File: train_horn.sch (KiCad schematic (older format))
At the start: 72 parts, among them J1 USB_OTG, J2 PROG, Q1 2N7002, SW1 PLAY, U1 MIC7221, U2 MCP73831, U3 TPS78233DDCR, U4 MSP430FR2000_TSSOP, U5 TPA6211A1

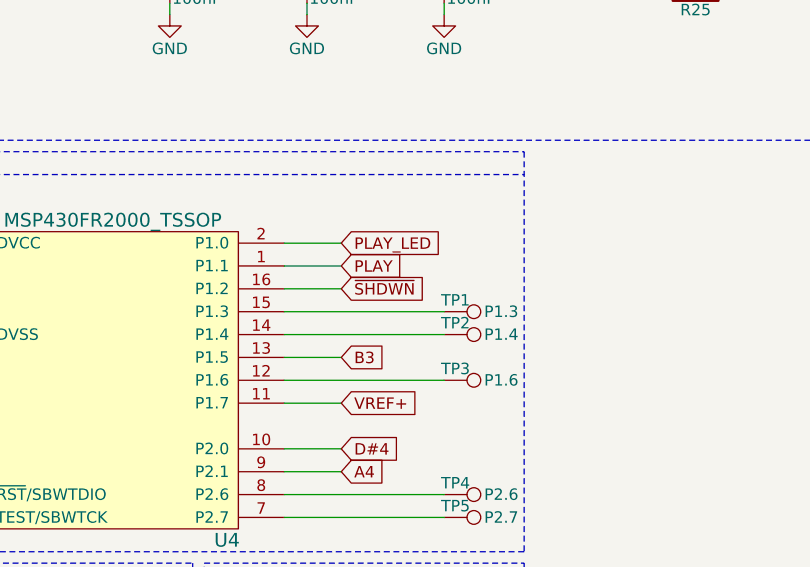
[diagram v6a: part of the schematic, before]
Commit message: move play button to P1.3 for PCB layout reasons
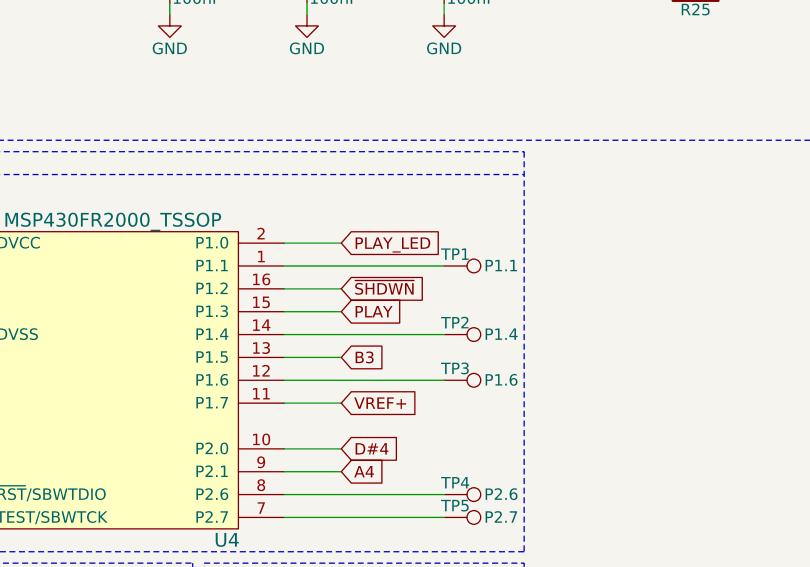
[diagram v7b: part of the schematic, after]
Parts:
- TP1: value P1.3 -> P1.1
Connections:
- net PLAY: now also U4.15 (P1.3); no longer U4.1 (P1.1)
- net at TP1.1: now also U4.1 (P1.1); no longer U4.15 (P1.3)
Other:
- moved on the sheet: TP1
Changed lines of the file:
@@
 Text GLabel 6600 3750 2    50   Input ~ 0
 PLAY_LED
-Text GLabel 6600 3850 2    50   Input ~ 0
+Text GLabel 6600 4050 2    50   Input ~ 0
 PLAY
 Text Notes 6000 5250 0    60   ~ 0
@@
 L Test_Point TP1
 U 1 1 5A824476
-P 7050 4050
-F 0 "TP1" V 7000 4100 50  0000 C CNN
-F 1 "P1.3" V 7050 4300 50  0000 C CNN
-F 2 "Connectors_TestPoints:Test_Point_Pad_d1.5mm" H 7250 4050 50  0001 C CNN
-F 3 "" H 7250 4050 50  0001 C CNN
-F 4 "NONE" H 7050 4050 60  0001 C CNN "Manufacture"
-F 5 "NONE" H 7050 4050 60  0001 C CNN "Mfg Part Number"
-F 6 "NONE" H 7050 4050 60  0001 C CNN "Package"
-F 7 "NONE" H 7050 4050 60  0001 C CNN "Description"
-	1    7050 4050
+P 7050 3850
+F 0 "TP1" V 7000 3900 50  0000 C CNN
+F 1 "P1.1" V 7050 4100 50  0000 C CNN
+F 2 "Connectors_TestPoints:Test_Point_Pad_d1.5mm" H 7250 3850 50  0001 C CNN
+F 3 "" H 7250 3850 50  0001 C CNN
+F 4 "NONE" H 7050 3850 60  0001 C CNN "Manufacture"
+F 5 "NONE" H 7050 3850 60  0001 C CNN "Mfg Part Number"
+F 6 "NONE" H 7050 3850 60  0001 C CNN "Package"
+F 7 "NONE" H 7050 3850 60  0001 C CNN "Description"
+	1    7050 3850
 	0    1    1    0
 $EndComp
@@
 	8750 1950 8800 1950
 Wire Wire Line
-	6350 3850 6600 3850
-Wire Wire Line
 	6450 5900 6800 5900
 Wire Wire Line
@@
 Wire Notes Line
 	6000 5150 7400 5150
-Wire Wire Line
-	6350 4050 7050 4050
 Wire Wire Line
 	7050 4150 6350 4150
@@
 Wire Wire Line
 	9800 1750 10100 1750
+Wire Wire Line
+	6350 4050 6600 4050
+Wire Wire Line
+	6350 3850 7050 3850
 $EndSCHEMATC

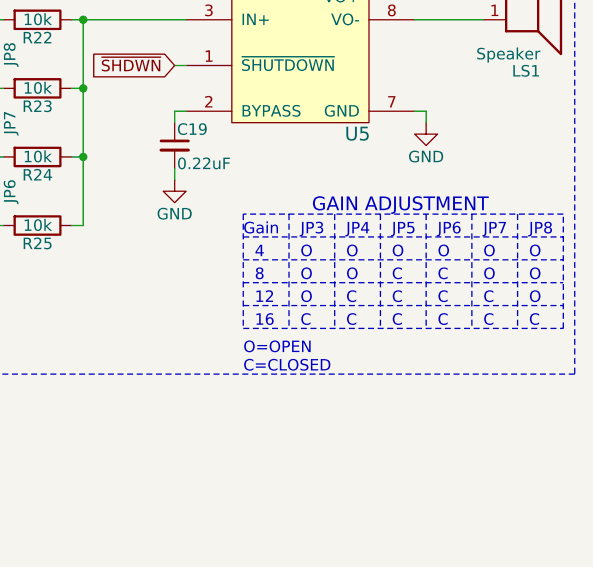
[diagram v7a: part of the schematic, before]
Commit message: finising touches on silkscreen
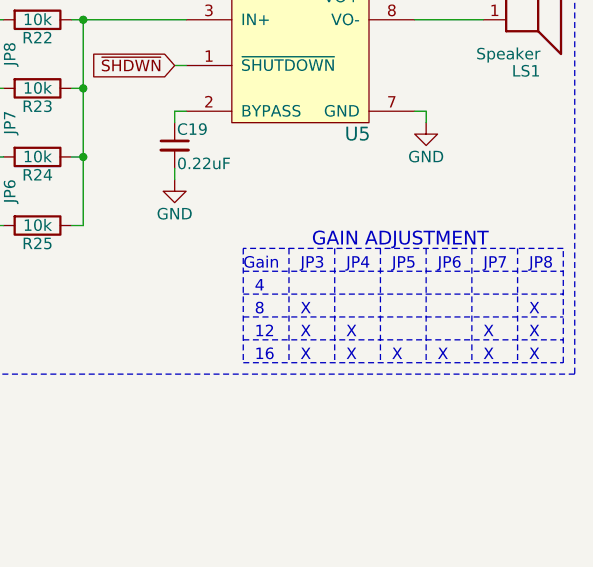
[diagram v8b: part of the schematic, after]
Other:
- note added: "X"
- note removed: "C"
- note removed: "O"
- note removed: "O=OPEN\nC=CLOSED"
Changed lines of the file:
@@
 	0    1    1    0
 $EndComp
-Text Notes 9050 2700 0    50   ~ 0
+Text Notes 9050 2850 0    50   ~ 0
 Gain
-Text Notes 9100 2800 0    50   ~ 0
+Text Notes 9100 2950 0    50   ~ 0
 4
-Text Notes 9100 2900 0    50   ~ 0
+Text Notes 9100 3050 0    50   ~ 0
 8
-Text Notes 9100 3000 0    50   ~ 0
+Text Notes 9100 3150 0    50   ~ 0
 12
-Text Notes 9100 3100 0    50   ~ 0
+Text Notes 9100 3250 0    50   ~ 0
 16
-Text Notes 9300 2700 0    50   ~ 0
+Text Notes 9300 2850 0    50   ~ 0
 JP3
-Text Notes 9700 2700 0    50   ~ 0
+Text Notes 9700 2850 0    50   ~ 0
 JP5
-Text Notes 9900 2700 0    50   ~ 0
+Text Notes 9900 2850 0    50   ~ 0
 JP6
-Text Notes 10100 2700 0    50   ~ 0
+Text Notes 10100 2850 0    50   ~ 0
 JP7
-Text Notes 10300 2700 0    50   ~ 0
+Text Notes 10300 2850 0    50   ~ 0
 JP8
-Text Notes 9300 2800 0    50   ~ 0
-O
-Text Notes 9500 2700 0    50   ~ 0
+Text Notes 9500 2850 0    50   ~ 0
 JP4
-Text Notes 9300 3100 0    50   ~ 0
-C
-Text Notes 9050 3300 0    50   ~ 0
-O=OPEN\nC=CLOSED
-Text Notes 9500 2800 0    50   ~ 0
-O
-Text Notes 9700 2800 0    50   ~ 0
-O
-Text Notes 9900 2800 0    50   ~ 0
-O
-Text Notes 10100 2800 0    50   ~ 0
-O
-Text Notes 10300 2800 0    50   ~ 0
-O
-Text Notes 9500 3100 0    50   ~ 0
-C
-Text Notes 9700 3100 0    50   ~ 0
-C
-Text Notes 9900 3100 0    50   ~ 0
-C
-Text Notes 10100 3100 0    50   ~ 0
-C
-Text Notes 10300 3100 0    50   ~ 0
-C
-Text Notes 9350 2600 0    60   ~ 0
+Text Notes 9300 3250 0    50   ~ 0
+X
+Text Notes 9500 3250 0    50   ~ 0
+X
+Text Notes 9700 3250 0    50   ~ 0
+X
+Text Notes 9900 3250 0    50   ~ 0
+X
+Text Notes 10100 3250 0    50   ~ 0
+X
+Text Notes 10300 3250 0    50   ~ 0
+X
+Text Notes 9350 2750 0    60   ~ 0
 GAIN ADJUSTMENT
-Text Notes 9700 2900 0    50   ~ 0
-C
-Text Notes 9900 2900 0    50   ~ 0
-C
-Text Notes 9700 3000 0    50   ~ 0
-C
-Text Notes 9900 3000 0    50   ~ 0
-C
-Text Notes 9500 3000 0    50   ~ 0
-C
-Text Notes 10100 3000 0    50   ~ 0
-C
-Text Notes 10100 2900 0    50   ~ 0
-O
-Text Notes 10300 2900 0    50   ~ 0
-O
-Text Notes 10300 3000 0    50   ~ 0
-O
-Text Notes 9500 2900 0    50   ~ 0
-O
-Text Notes 9300 2900 0    50   ~ 0
-O
-Text Notes 9300 3000 0    50   ~ 0
-O
+Text Notes 9500 3150 0    50   ~ 0
+X
+Text Notes 10100 3150 0    50   ~ 0
+X
+Text Notes 9300 3150 0    50   ~ 0
+X
 Wire Wire Line
 	4250 3750 4850 3750
@@
 Connection ~ 8350 1750
 Wire Notes Line
-	9050 2700 10450 2700
-Wire Notes Line
-	10250 2600 10250 3100
-Wire Notes Line
-	10050 2600 10050 3100
-Wire Notes Line
-	9850 2600 9850 3100
-Wire Notes Line
-	9650 2600 9650 3100
-Wire Notes Line
-	9450 2600 9450 3100
-Wire Notes Line
-	9250 2600 9250 3100
-Wire Notes Line
-	9050 2600 9050 3100
-Wire Notes Line
-	9050 3100 10450 3100
-Wire Notes Line
-	10450 3100 10450 2600
-Wire Notes Line
-	10450 2600 9050 2600
-Wire Notes Line
-	9050 2800 10450 2800
-Wire Notes Line
-	9050 2900 10450 2900
-Wire Notes Line
-	9050 3000 10450 3000
+	9050 2850 10450 2850
+Wire Notes Line
+	10250 2750 10250 3250
+Wire Notes Line
+	10050 2750 10050 3250
+Wire Notes Line
+	9850 2750 9850 3250
+Wire Notes Line
+	9650 2750 9650 3250
+Wire Notes Line
+	9450 2750 9450 3250
+Wire Notes Line
+	9250 2750 9250 3250
+Wire Notes Line
+	9050 2750 9050 3250
+Wire Notes Line
+	9050 3250 10450 3250
+Wire Notes Line
+	10450 3250 10450 2750
+Wire Notes Line
+	10450 2750 9050 2750
+Wire Notes Line
+	9050 2950 10450 2950
+Wire Notes Line
+	9050 3050 10450 3050
+Wire Notes Line
+	9050 3150 10450 3150
 Wire Wire Line
 	9800 1650 10100 1650
@@
 Wire Wire Line
 	6350 3850 7050 3850
+Text Notes 9300 3050 0    50   ~ 0
+X
+Text Notes 10300 3150 0    50   ~ 0
+X
+Text Notes 10300 3050 0    50   ~ 0
+X
 $EndSCHEMATC
